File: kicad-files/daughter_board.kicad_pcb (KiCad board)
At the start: 2 copper layers, 14 parts, among them J1 TYPE-C-31-M12_13, T1 53261-0471, U2 USBLC6-2SC6, U4 SGM2007-3.3XN5/TR

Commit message: SMall changes to the db
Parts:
- moved J1 79.4 mm to (120.0, 34.1), turned to 180 degrees
- moved T1 79.4 mm to (120.0, 54.0)
- moved U2 70.8 mm to (118.9, 44.0)
- moved C3 30.9 mm to (79.9, 60.0)
- moved C4 30.9 mm to (79.9, 62.5)
- moved C5 30.9 mm to (79.9, 65.0)
- moved F1 28.7 mm to (64.0, 63.0)
- moved D1 28.5 mm to (72.0, 57.0)
- moved R4 28.0 mm to (73.0, 66.5)
- moved R3 28.0 mm to (73.0, 64.0)
- moved U4 23.4 mm to (64.0, 57.0)
- moved R2 23.2 mm to (27.0, 40.0), turned to 90 degrees
- moved R1 17.7 mm to (32.0, 40.0), turned to -90 degrees
- moved FB1 13.1 mm to (38.0, 39.0), turned to -90 degrees
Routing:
- net Net-(J1-D+-PadA6): track 0.00 -> 7.18 mm
- net Net-(J1-D--PadA7): track 0.00 -> 6.97 mm, vias 0 -> 2

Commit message: Fixed up the daughter board
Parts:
- removed U2: USBLC6-2SC6, acheron_Components:SOT-23-6
- added D2: B5819W-SL, Diode_SMD:D_SOD-123, F.Cu at (105.0, 54.5)
- added U1: TPD4E05U06DQAR, Package_SON:USON-10_2.5x1.0mm_P0.5mm, F.Cu at (120.0, 43.0)
- D1: value B5819W-SL -> ESD5Z5V0; footprint Diode_SMD:D_SOD-123 -> Diode_SMD:D_SOD-523
- moved R1 91.3 mm to (123.2, 38.2), turned to 0 degrees
- moved R2 89.8 mm to (116.8, 38.2), turned to 180 degrees
- moved FB1 75.8 mm to (113.8, 36.0), turned to 90 degrees
- moved F1 50.8 mm to (110.3, 42.0)
- moved D1 37.4 mm to (104.5, 38.5)
- moved U4 9.26 mm to (73.2, 56.5)
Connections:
- C5 pad 1: Net-(D1-A) -> 3V3
- D1 pad 1: 5V -> GND
- D1 pad 2: Net-(D1-A) -> VBUS
- F1 pad 1: Net-(U2-VBUS) -> VBUS
- J1 pad A4: Net-(U2-VBUS) -> VBUS
- J1 pad A6: Net-(J1-D+-PadA6) -> D+
- J1 pad A7: Net-(J1-D--PadA7) -> D-
- J1 pad B4: Net-(U2-VBUS) -> VBUS
- J1 pad B6: Net-(J1-D+-PadA6) -> D+
- J1 pad B7: Net-(J1-D--PadA7) -> D-
- R4 pad 2: Net-(D1-A) -> 3V3
- T1 pad 1: Net-(D1-A) -> 3V3
- T1 pad 2: Net-(T1-D+) -> D+
- T1 pad 3: Net-(T1-D-) -> D-
- U4 pad 5: Net-(D1-A) -> 3V3
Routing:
- net GNDPWR: track 0.00 -> 20.0 mm
- net VBUS: track 0.00 -> 16.2 mm, vias 0 -> 3
- net D+: track 0.00 -> 12.8 mm, vias 0 -> 2
- net D-: track 0.00 -> 11.1 mm, vias 0 -> 2
- net Net-(J1-D+-PadA6): track 7.18 -> 0.00 mm
- net Net-(J1-D--PadA7): track 6.97 -> 0.00 mm, vias 2 -> 0
- net Net-(J1-CC1): track 0.00 -> 5.34 mm
- net Net-(J1-CC2): track 0.00 -> 5.13 mm
- net GND: track 0.00 -> 4.91 mm, vias 0 -> 2
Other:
- rule pad_to_mask_clearance: 0 -> 0.1

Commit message: Finished daughter board
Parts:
- added MH1: Mount-M2, MountingHole:MountingHole_2.2mm_M2_Pad_TopOnly, F.Cu at (91.5, 80.8)
- added MH2: Mount-M2, MountingHole:MountingHole_2.2mm_M2_Pad_TopBottom, F.Cu at (108.5, 80.8)
- added MH3: Mount-M2, MountingHole:MountingHole_2.2mm_M2_Pad_TopOnly, F.Cu at (91.5, 100.5)
- added MH4: Mount-M2, MountingHole:MountingHole_2.2mm_M2_Pad_TopOnly, F.Cu at (108.5, 100.5)
- C3, C4, C5: footprint Capacitor_SMD:C_0603_1608Metric_Pad1.08x0.95mm_HandSolder -> Capacitor_SMD:C_0402_1005Metric
- D2: value B5819W-SL -> 1N5819WS
- R1, R2, R3, R4: footprint Resistor_SMD:R_0603_1608Metric -> Resistor_SMD:R_0402_1005Metric
- moved J1 55.0 mm to (100.0, 85.3)
- moved R1 53.4 mm to (102.9, 87.6)
- moved R2 53.1 mm to (97.1, 87.6)
- moved D1 51.4 mm to (103.1, 89.9), turned to 180 degrees
- moved U1 50.8 mm to (100.0, 89.7), turned to 90 degrees
- moved FB1 50.6 mm to (108.0, 86.2), turned to -90 degrees
- moved F1 50.4 mm to (104.0, 92.0)
- moved T1 49.1 mm to (100.0, 98.8)
- moved R3 42.9 mm to (103.1, 94.6), turned to 90 degrees
- moved C3 42.5 mm to (104.6, 94.6), turned to -90 degrees
- moved D2 40.9 mm to (92.4, 93.4), turned to -90 degrees
- moved U4 40.8 mm to (95.6, 90.6), turned to -90 degrees
- moved R4 36.6 mm to (97.2, 94.0), turned to 180 degrees
- moved C5 35.0 mm to (97.2, 95.4)
- moved C4 34.7 mm to (94.7, 93.9), turned to -90 degrees
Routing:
- net 5V: track 0.00 -> 20.0 mm, vias 0 -> 2
- net D-: track 11.1 -> 25.6 mm, vias 2 -> 4
- net 3V3: track 0.00 -> 11.7 mm
- net D+: track 12.8 -> 22.6 mm
- net GND: track 4.91 -> 9.64 mm, vias 2 -> 4
- net Net-(J1-CC2): track 5.13 -> 3.27 mm
- net Net-(J1-CC1): track 5.34 -> 3.47 mm
- net Net-(U4-BP/FB): track 0.00 -> 1.69 mm
- net GNDPWR: track 20.0 -> 21.6 mm
- net VBUS: track 16.2 -> 15.5 mm
- added copper zone on B.Cu, net GND
- added copper zone on F.Cu, net GND
- added copper zone on F.Cu, net GNDPWR
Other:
- board outline added: 22 x 24.8 mm
- rule pad_to_mask_clearance: 0.1 -> 0

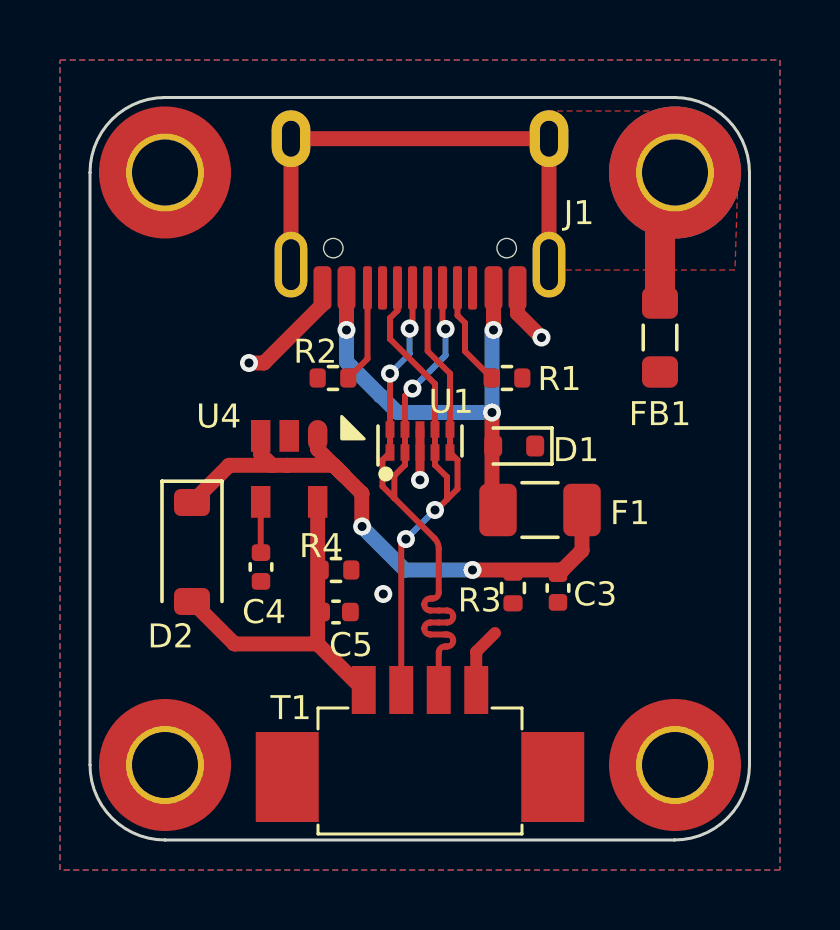
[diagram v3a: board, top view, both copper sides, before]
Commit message: Fixed the boards edge cuts
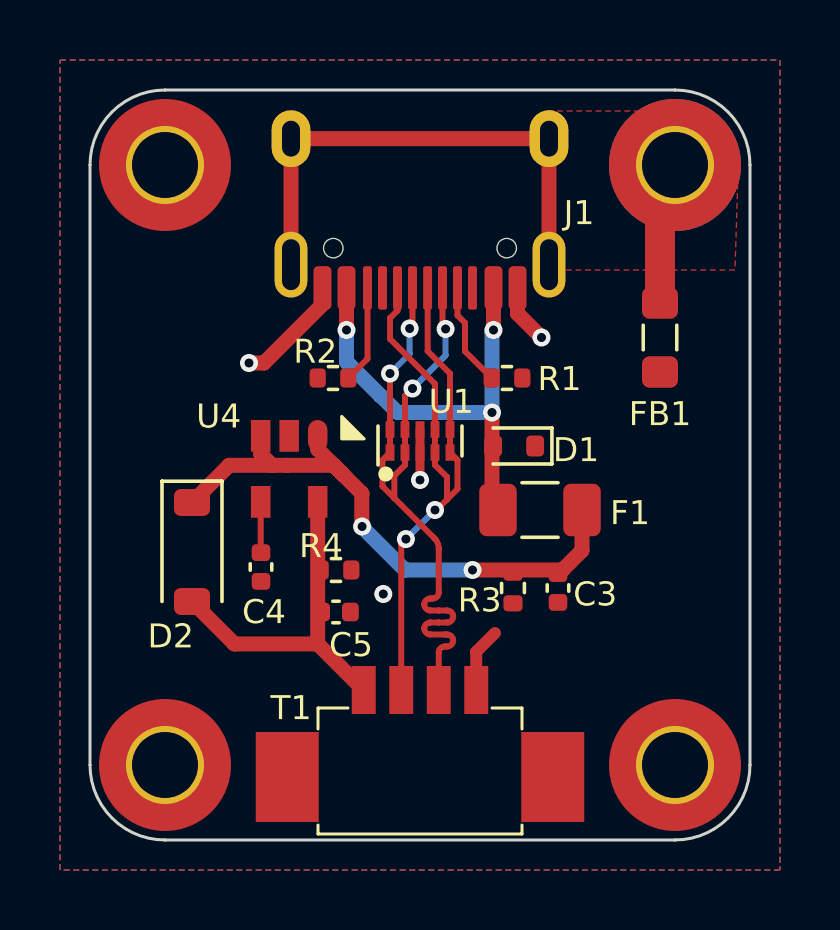
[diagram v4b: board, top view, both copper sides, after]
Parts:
- moved MH1 0.25 mm to (91.5, 80.5)
- moved MH2 0.25 mm to (108.5, 80.5)
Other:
- board size 22 x 24.8 mm -> 22 x 25 mm
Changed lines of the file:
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@@
     )
     (pad_to_mask_clearance 0)
+    (aux_axis_origin 91.5 80.517767)
     (pcbplotparams
       (layerselection 0x00010fc_ffffffff)
@@
   )
   (footprint "MountingHole:MountingHole_2.2mm_M2_Pad_TopOnly" (layer "F.Cu")
-    (at 91.5 80.75)
+    (at 91.5 80.5)
     (descr "Mounting Hole 2.2mm, M2")
     (tags "mounting hole 2.2mm m2")
@@
   )
   (footprint "MountingHole:MountingHole_2.2mm_M2_Pad_TopBottom" (layer "F.Cu")
-    (at 108.5 80.75)
+    (at 108.5 80.5)
     (descr "Mounting Hole 2.2mm, M2")
     (tags "mounting hole 2.2mm m2")
@@
     )
   )
+  (gr_line (start 91.5 78) (end 108.5 78)
+    (stroke (width 0.1) (type default)) (layer "Edge.Cuts"))
   (gr_arc (start 91.5 103) (mid 89.732233 102.267767) (end 89 100.5)
     (stroke (width 0.1) (type default)) (layer "Edge.Cuts"))
-  (gr_arc (start 108.482786 78.25) (mid 110.250562 78.982228) (end 110.982786 80.75)
+  (gr_line (start 111 80.5) (end 111 100.5)
     (stroke (width 0.1) (type default)) (layer "Edge.Cuts"))
-  (gr_arc (start 110.982786 100.5) (mid 110.250553 102.267767) (end 108.482786 103)
+  (gr_arc (start 108.5 78) (mid 110.267767 78.732233) (end 111 80.5)
     (stroke (width 0.1) (type default)) (layer "Edge.Cuts"))
-  (gr_line (start 89 100.5) (end 89 80.75)
+  (gr_arc (start 89 80.5) (mid 89.732233 78.732233) (end 91.5 78)
     (stroke (width 0.1) (type default)) (layer "Edge.Cuts"))
-  (gr_line (start 110.982786 80.75) (end 110.982786 100.5)
+  (gr_line (start 89 100.5) (end 89 80.5)
     (stroke (width 0.1) (type default)) (layer "Edge.Cuts"))
-  (gr_line (start 91.5 78.25) (end 108.482786 78.25)
+  (gr_line (start 108.5 103) (end 91.5 103)
     (stroke (width 0.1) (type default)) (layer "Edge.Cuts"))
-  (gr_line (start 108.482786 103) (end 91.5 103)
-    (stroke (width 0.1) (type default)) (layer "Edge.Cuts"))
-  (gr_arc (start 89 80.75) (mid 89.732233 78.982233) (end 91.5 78.25)
+  (gr_arc (start 111 100.5) (mid 110.267767 102.267767) (end 108.5 103)
     (stroke (width 0.1) (type default)) (layer "Edge.Cuts"))
   (segment (start 98.07 91.455) (end 97.4275 90.8125) (width 0.5) (layer "F.Cu") (net 1))

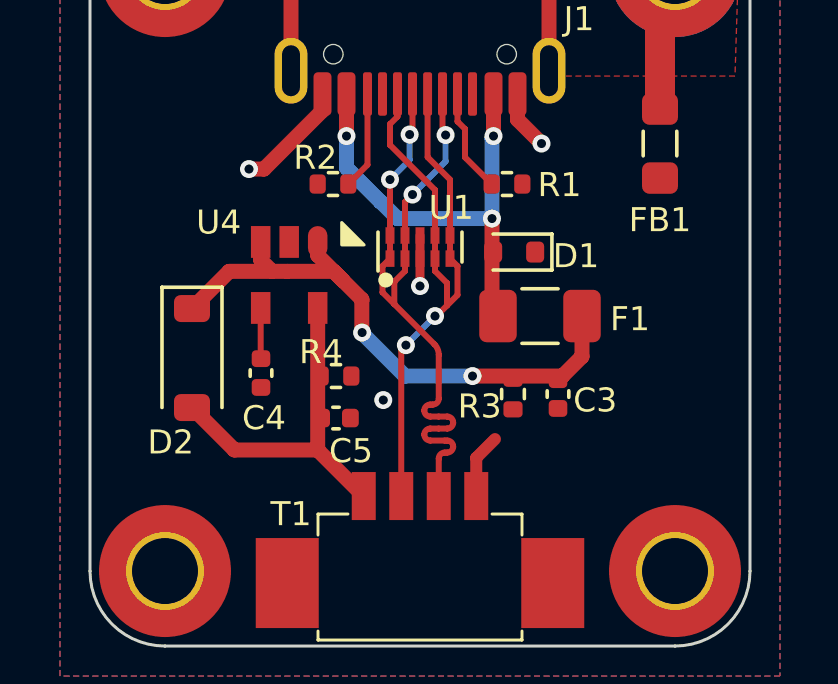
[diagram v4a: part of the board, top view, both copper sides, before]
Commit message: Fixing up the schematic's of daughter and mother boards
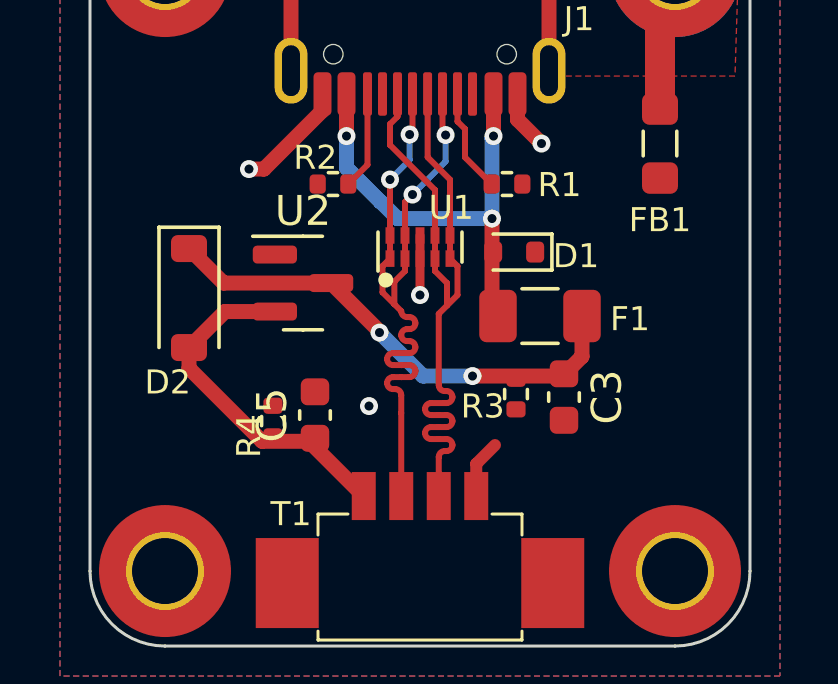
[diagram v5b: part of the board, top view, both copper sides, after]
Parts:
- removed C4: 10n, Capacitor_SMD:C_0402_1005Metric
- removed U4: SGM2007-3.3XN5/TR, acheron_Components:SOT-23-5
- added U2: MCP1700T-3302E/TT, Package_TO_SOT_SMD:SOT-23, F.Cu at (96.1, 90.9)
- C3, C5: footprint Capacitor_SMD:C_0402_1005Metric -> Capacitor_SMD:C_0603_1608Metric
- moved R4 2.58 mm to (95.1, 95.5), turned to -90 degrees
- moved D2 2.00 mm to (92.3, 91.4)
- moved C5 0.71 mm to (96.5, 95.3), turned to 90 degrees
- moved C3 0.22 mm to (104.8, 94.7)
- moved R3 0.10 mm to (103.2, 94.6)
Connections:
- T1 pad 2: D+ -> D-
- T1 pad 3: D- -> D+
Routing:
- net 5V: track 20.0 -> 16.5 mm
- net D+: track 22.6 -> 25.5 mm, vias 2 -> 0
- net Net-(U4-BP/FB): track 1.69 -> 0.00 mm

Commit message: More small tweaks to the daughter boardd
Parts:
- moved D2 1.71 mm to (92.5, 93.1)
- moved R4 0.30 mm to (94.8, 95.5)
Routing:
- net 3V3: track 11.6 -> 6.97 mm
- net D+: track 25.5 -> 22.0 mm
- net D-: track 25.5 -> 22.3 mm
- net GND: vias 4 -> 6

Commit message: Added legshark logo to the daugherboard
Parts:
- added H1: LegSharkLogo, Legshark:Legshark_Small_Mask, F.Cu at (92.2, 86.6)
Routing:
- net 3V3: track 6.97 -> 11.3 mm
- net GND: track 9.74 -> 7.96 mm
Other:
- board text added: "Legshark65 DB"
- board text added: "Version 1.0"

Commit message: Added parts
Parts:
- moved D1 0.06 mm to (103.2, 89.9), turned to 0 degrees
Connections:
- D1 pad 1: GND -> VBUS
- D1 pad 2: VBUS -> GND
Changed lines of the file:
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@@
   )
   (footprint "Diode_SMD:D_SOD-523" (layer "F.Cu")
-    (at 103.137675 89.867195 180)
+    (at 103.2 89.867195)
     (descr "http://www.diodes.com/datasheets/ap02001.pdf p.144")
     (tags "Diode SOD523")
@@
     (property "ki_keywords" "diode TVS voltage suppressor")
     (attr smd)
-    (fp_text reference "D1" (at -2.262325 0.067195) (layer "F.SilkS")
+    (fp_text reference "D1" (at 2.2 0.067195) (layer "F.SilkS")
         (effects (font (size 0.9 0.9) (thickness 0.15)))
     )
@@
     (fp_line (start 0.65 0.45) (end -0.65 0.45)
       (stroke (width 0.1) (type solid)) (layer "F.Fab"))
-    (pad "1" smd roundrect (at -0.7 0) (size 0.6 0.7) (layers "F.Cu" "F.Paste" "F.Mask") (roundrect_rratio 0.25)
-      (net 2 "GND") (pinfunction "A1") (pintype "passive"))
-    (pad "2" smd roundrect (at 0.7 0) (size 0.6 0.7) (layers "F.Cu" "F.Paste" "F.Mask") (roundrect_rratio 0.25)
-      (net 9 "VBUS") (pinfunction "A2") (pintype "passive"))
+    (pad "1" smd roundrect (at -0.7 0 180) (size 0.6 0.7) (layers "F.Cu" "F.Paste" "F.Mask") (roundrect_rratio 0.25)
+      (net 9 "VBUS") (pinfunction "A1") (pintype "passive"))
+    (pad "2" smd roundrect (at 0.7 0 180) (size 0.6 0.7) (layers "F.Cu" "F.Paste" "F.Mask") (roundrect_rratio 0.25)
+      (net 2 "GND") (pinfunction "A2") (pintype "passive"))
     (model "${KICAD6_3DMODEL_DIR}/Diode_SMD.3dshapes/D_SOD-523.wrl"
       (offset (xyz 0 0 0))
